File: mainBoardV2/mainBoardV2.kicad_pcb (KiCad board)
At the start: 2 copper layers, 55.9 x 117 mm, 28 parts, among them J1 USB4125-GF-A_REVA2, U2 ESP32-DEVKITC-32E, U3 MCP73871-2AAI_ML, U4 MPU6050_Module, U5 TPS61023DRLT

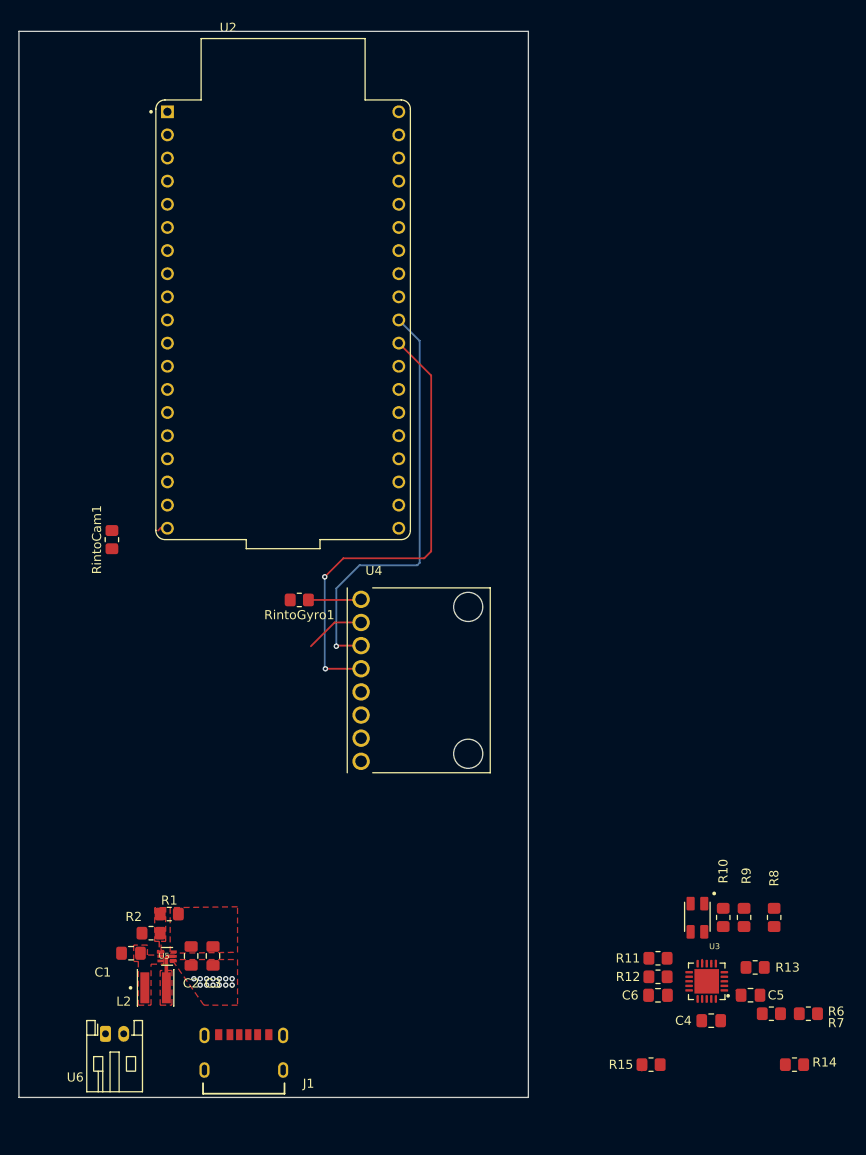
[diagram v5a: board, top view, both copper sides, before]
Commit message: 3.11.26.C2
Connected up the capacitors in the charging circuit.
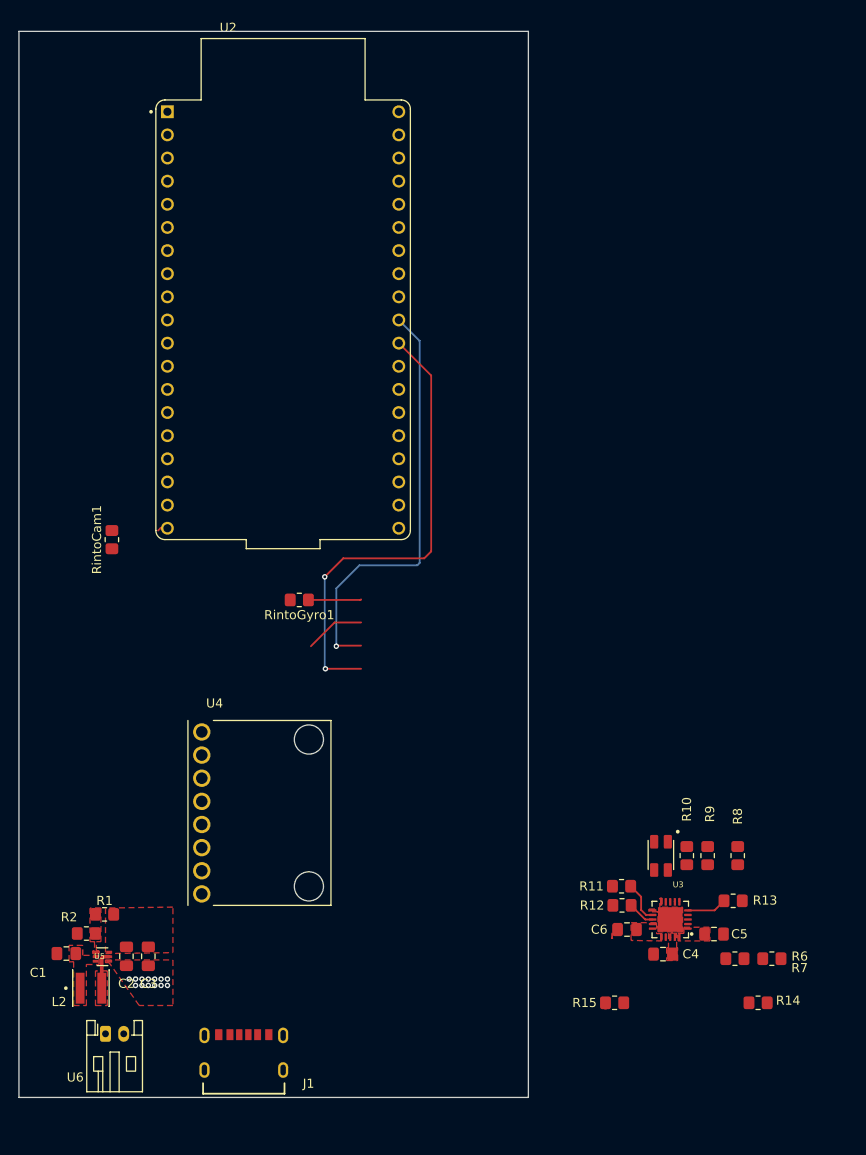
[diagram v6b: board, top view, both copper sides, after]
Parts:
- moved U4 22.8 mm to (108.4, 97.8)
- moved C4 9.02 mm to (152.7, 113.3), turned to 180 degrees
- moved R11 8.86 mm to (148.2, 105.8)
- moved R12 8.78 mm to (148.2, 108.0)
- moved C6 7.98 mm to (148.8, 110.6)
- moved R10 7.88 mm to (155.3, 102.5)
- moved R14 7.88 mm to (163.1, 118.6)
- moved R15 7.88 mm to (147.4, 118.6)
- moved R8 7.88 mm to (160.9, 102.5)
- moved R9 7.88 mm to (157.6, 102.5)
- moved U3 7.88 mm to (153.5, 109.5)
- moved U7 7.88 mm to (151.7, 101.0)
- moved C5 7.82 mm to (158.3, 111.1)
- moved R13 7.70 mm to (160.4, 107.5), turned to 180 degrees
- moved R7 7.25 mm to (164.7, 113.8)
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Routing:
- net (no net): track 104.1 -> 0.00 mm, vias 3 -> 0
- net unconnected-(U2-IO17-PadJ3_11): track 0.00 -> 51.3 mm, vias 0 -> 2
- net unconnected-(U2-IO5-PadJ3_10): track 0.00 -> 47.0 mm, vias 0 -> 1
- net unconnected-(RintoGyro1-Pad1): track 0.00 -> 5.81 mm
- net /PROG3: track 0.00 -> 4.57 mm
- net /Therm: track 0.69 -> 5.09 mm
- net /PROG1: track 0.70 -> 3.01 mm
- net /VoutCharger: track 0.76 -> 0.02 mm
- added copper zone on F.Cu, net /5VUSB
- added copper zone on F.Cu, net /VoutCharger

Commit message: 3.11.26.C3
Post meeting with Deepika and some group discussion, removing ESP32 from schemactic and breadboard. Moved some components closer together to get a rough estimate for board size so we can start designing a housing.
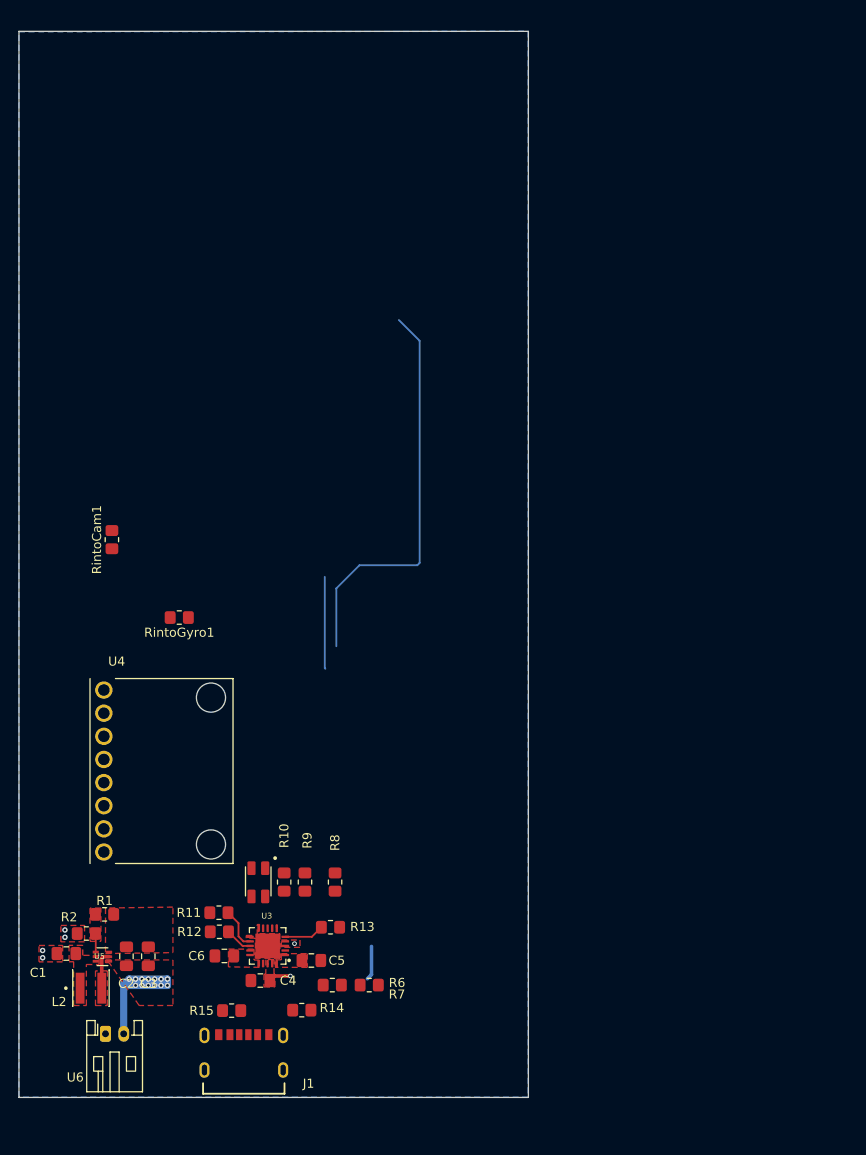
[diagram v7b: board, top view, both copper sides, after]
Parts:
- removed U2: ESP32-DEVKITC-32E, ESP32-DEVKITC-32E:MODULE_ESP32-DEVKITC-32E
- moved R14 50.1 mm to (113.0, 119.5)
- moved C5 44.3 mm to (114.1, 114.0)
- moved R9 44.3 mm to (113.4, 105.4)
- moved C6 44.3 mm to (104.5, 113.5)
- moved R10 44.3 mm to (111.1, 105.4)
- moved R11 44.3 mm to (104.0, 108.8)
- moved R13 44.3 mm to (116.2, 110.3)
- moved R6 44.3 mm to (116.4, 116.7)
- moved R7 44.3 mm to (120.5, 116.7)
- moved R8 44.3 mm to (116.7, 105.4)
- moved U3 44.3 mm to (109.3, 112.4)
- moved C4 44.3 mm to (108.5, 116.2)
- moved R12 44.3 mm to (104.0, 110.8)
- moved U7 44.3 mm to (107.5, 103.9)
- moved R15 42.0 mm to (105.3, 119.5)
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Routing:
- net unconnected-(U2-IO17-PadJ3_11): track 51.3 -> 10.1 mm, vias 2 -> 0
- net GND: track 1.68 -> 16.7 mm, vias 13 -> 17
- net unconnected-(U4-PadGND): track 6.59 -> 0.00 mm
- net /5VUSB: track 0.01 -> 6.26 mm, vias 0 -> 2
- net unconnected-(RintoGyro1-Pad1): track 5.81 -> 0.00 mm
- net unconnected-(U2-IO5-PadJ3_10): track 47.0 -> 44.3 mm, vias 1 -> 0
- net /Boost FB: track 0.00 -> 2.06 mm
- net unconnected-(U2-EXT_5V-PadJ2_19): track 1.12 -> 0.00 mm
- added copper zone on B.Cu, net GND
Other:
- board text removed: "ON/OFF here"

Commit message: 3.11.26.C4
Finalized copper connections and placed ground vias. Got closer to final size goal of 50x50 mm (2x2in). Placed ground vias, and placed thick traces on power connections.
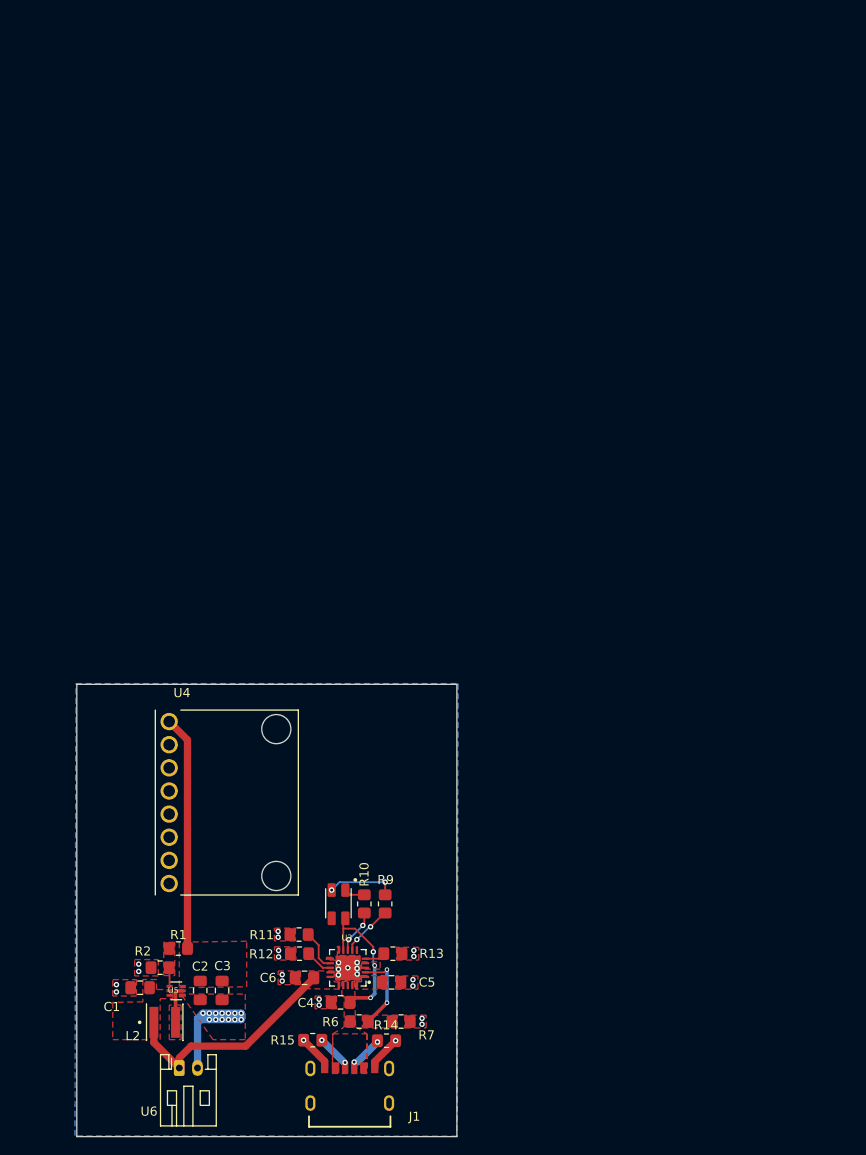
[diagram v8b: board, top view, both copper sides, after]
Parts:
- removed R8: 470k, Resistor_SMD:R_0805_2012Metric_Pad1.20x1.40mm_HandSolder
- removed RintoCam1, RintoGyro1: R, Resistor_SMD:R_0805_2012Metric_Pad1.20x1.40mm_HandSolder
- moved J1 12.2 mm to (118.3, 128.8)
- moved R14 9.88 mm to (122.3, 122.8)
- moved R15 9.47 mm to (114.2, 122.8)
- moved C5 9.12 mm to (122.9, 116.4)
- moved R9 9.12 mm to (122.2, 107.8), turned to 90 degrees
- moved C6 9.12 mm to (113.3, 115.9)
- moved R10 9.12 mm to (119.9, 107.8), turned to 90 degrees
- moved R11 9.12 mm to (112.8, 111.2)
- moved R12 9.12 mm to (112.8, 113.2)
- moved C4 9.12 mm to (117.3, 118.6)
- moved U3 9.12 mm to (118.1, 114.8)
- moved U7 9.12 mm to (116.3, 106.3)
- moved C2 8.93 mm to (101.9, 117.3)
- moved C1 8.93 mm to (95.3, 117.0)
- moved C3 8.93 mm to (104.3, 117.3)
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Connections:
- C4 pad 1: /5VUSB -> +5V
- C5 pad 1: /VoutCharger -> /VoutBoost
- R6 pad 1: /5VUSB -> +5V
- U3 pad 1: /VoutCharger -> /VoutBoost
- U3 pad 17: /5VUSB -> +5V
- U3 pad 18: /5VUSB -> +5V
- U3 pad 19: /5VUSB -> +5V
- U3 pad 20: /VoutCharger -> /VoutBoost
- U3 pad 3: /5VUSB -> +5V
- U3 pad 4: /5VUSB -> +5V
- U3 pad 9: /5VUSB -> +5V
- U4 pad VCC: unconnected-(U4-PadVCC) -> /VoutBoost
- U7 pad 4: /5VUSB -> +5V
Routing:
- net unconnected-(U2-IO5-PadJ3_10): track 44.3 -> 0.00 mm
- net /VoutBoost: track 0.00 -> 25.8 mm
- net /VBatt+: track 0.00 -> 25.7 mm
- net +5V: track 0.00 -> 16.1 mm, vias 0 -> 3
- net unconnected-(U2-IO17-PadJ3_11): track 10.1 -> 0.00 mm
- net /VPCC: track 0.00 -> 9.04 mm, vias 0 -> 2
- net GND: track 16.7 -> 24.6 mm, vias 17 -> 40
- net Net-(U7-Green): track 0.05 -> 7.66 mm, vias 0 -> 2
- net /5VUSB: track 6.26 -> 0.00 mm, vias 2 -> 0
- net /ChargeDone: track 0.10 -> 5.68 mm, vias 0 -> 2
- net /LowBatt: track 0.27 -> 4.83 mm, vias 0 -> 2
- net Net-(J1-CC1): track 0.00 -> 3.60 mm, vias 0 -> 2
- net Net-(J1-CC2): track 0.00 -> 3.49 mm, vias 0 -> 2
- net /Therm: track 5.09 -> 2.24 mm
- net Net-(U7-Red): track 0.00 -> 2.57 mm
- added copper zone on F.Cu, net +5V
- added copper zone on F.Cu, net /VPCC
- removed copper zone on F.Cu, net /5VUSB
- removed copper zone on F.Cu, net /VoutCharger
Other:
- board size 55.9 x 117 mm -> 41.7 x 49.6 mm
- board text added: "ON/OFF here"
